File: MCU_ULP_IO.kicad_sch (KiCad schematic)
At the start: 2 parts, among them U11 SiWG917Y

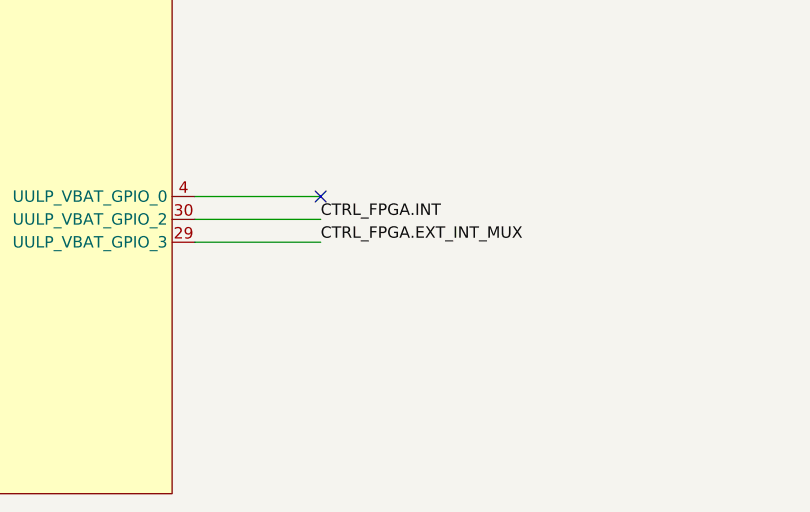
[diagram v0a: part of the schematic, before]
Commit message: added schematics comments of review 1
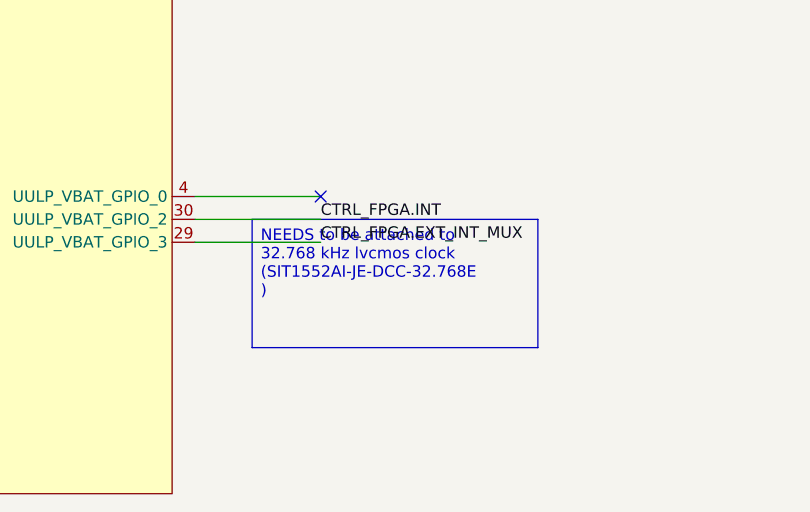
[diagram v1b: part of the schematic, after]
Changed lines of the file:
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@@
 	(generator_version "10.0")
 	(paper "A4")
+	(text_box "NEEDS to be attached to 32.768 kHz lvcmos clock (SIT1552AI-JE-DCC-32.768E\n)"
+		(exclude_from_sim no)
+		(at 177.8 91.44 0)
+		(size 31.75 14.2494)
+		(margins 0.9525 0.9525 0.9525 0.9525)
+		(stroke
+			(width 0)
+			(type solid)
+		)
+		(fill
+			(type color)
+			(color 255 153 0 1)
+		)
+		(effects
+			(font
+				(size 1.27 1.27)
+			)
+			(justify left top)
+		)
+	)
 	(junction
 		(at 116.84 55.88)

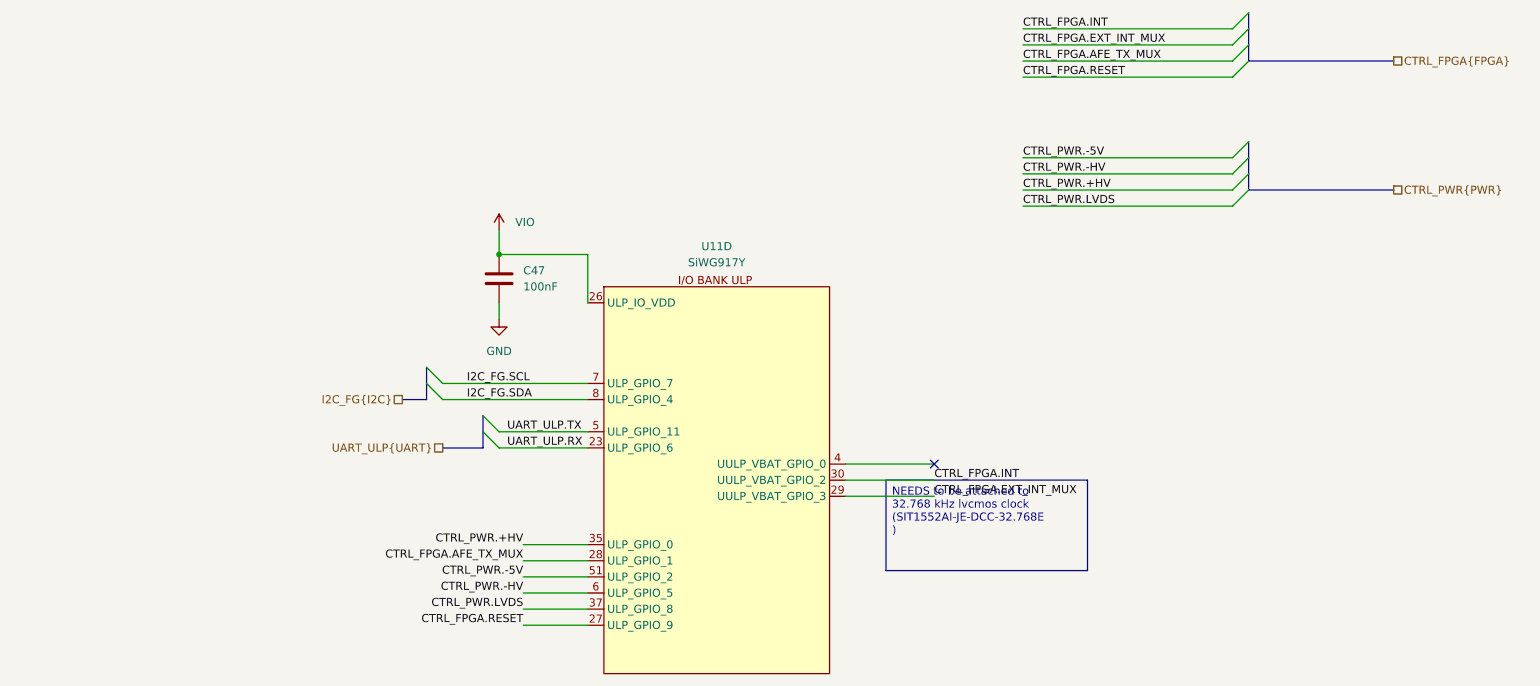
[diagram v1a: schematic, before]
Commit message: changes after first review: add lvl shifters, board at 1v8, new power tree
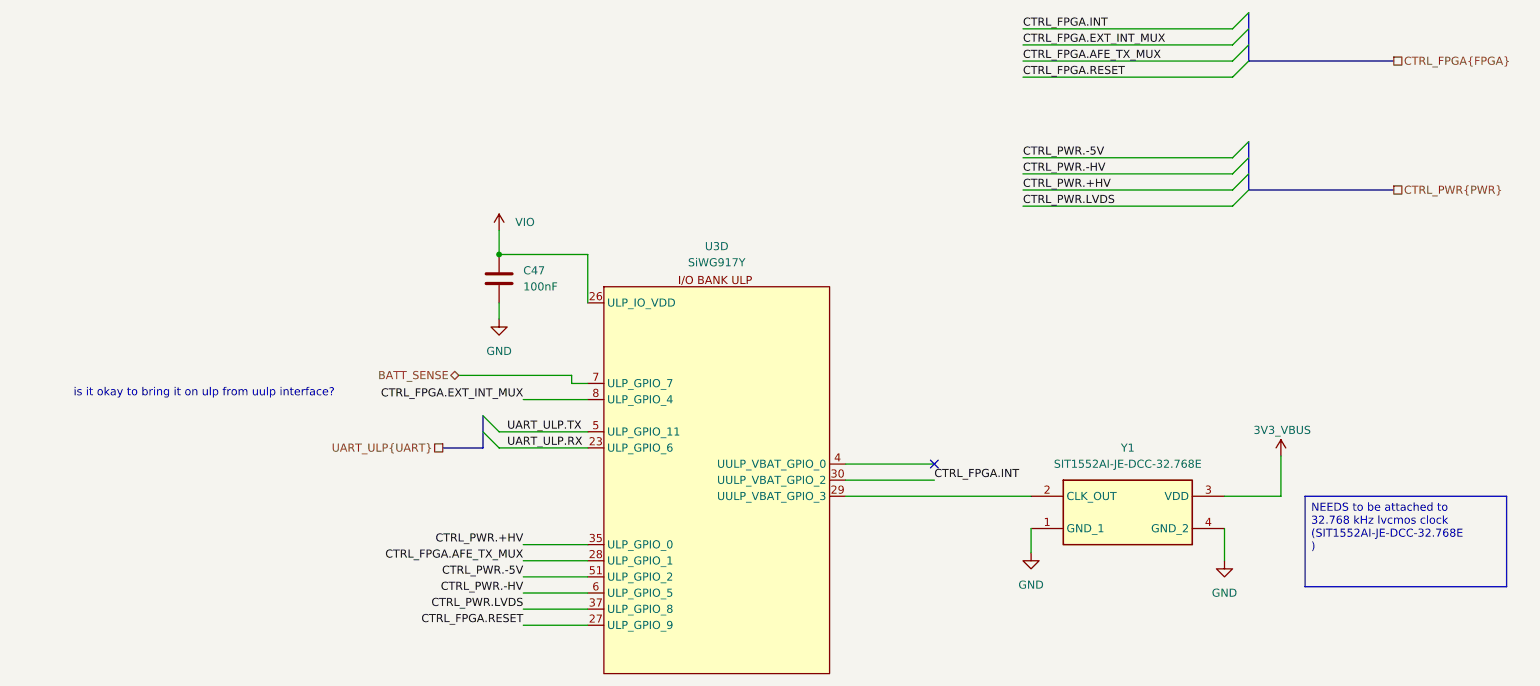
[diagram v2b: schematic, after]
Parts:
- added Y1: SIT1552AI-JE-DCC-32.768E, dz_sens:SIT1552AIJEDCC32768E, symbol #dzdb:s_clk/XTL-SI-SIT1552-32.768kHz
- renumbered U11 to U3
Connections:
- net I2C_FG.SDA is gone; now on net CTRL_FPGA.EXT_INT_MUX: U3.8 (ULP_GPIO_4)
- net CTRL_FPGA.EXT_INT_MUX: no longer U3.29 (UULP_VBAT_GPIO_3)
- net GND: now also Y1.1 (GND_1), Y1.4 (GND_2)
- net I2C_FG.SCL renamed BATT_SENSE
- new net: U3.29 (UULP_VBAT_GPIO_3), Y1.2 (CLK_OUT)
- new net 3V3_VBUS: Y1.3 (VDD)
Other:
- note added: "is it okay to bring it on ulp from uulp interface?"

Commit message: updated schematic and initial pcb placement
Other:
- note removed: "is it okay to bring it on ulp from uulp interface?"
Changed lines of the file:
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@@
 	(generator_version "10.0")
 	(paper "A4")
-	(text "is it okay to bring it on ulp from uulp interface?\n"
-		(exclude_from_sim no)
-		(at 70.358 77.724 0)
-		(effects
-			(font
-				(size 1.27 1.27)
-			)
-		)
-	)
 	(text_box "NEEDS to be attached to 32.768 kHz lvcmos clock (SIT1552AI-JE-DCC-32.768E\n)"
 		(exclude_from_sim no)
